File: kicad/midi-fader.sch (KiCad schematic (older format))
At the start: 0 parts

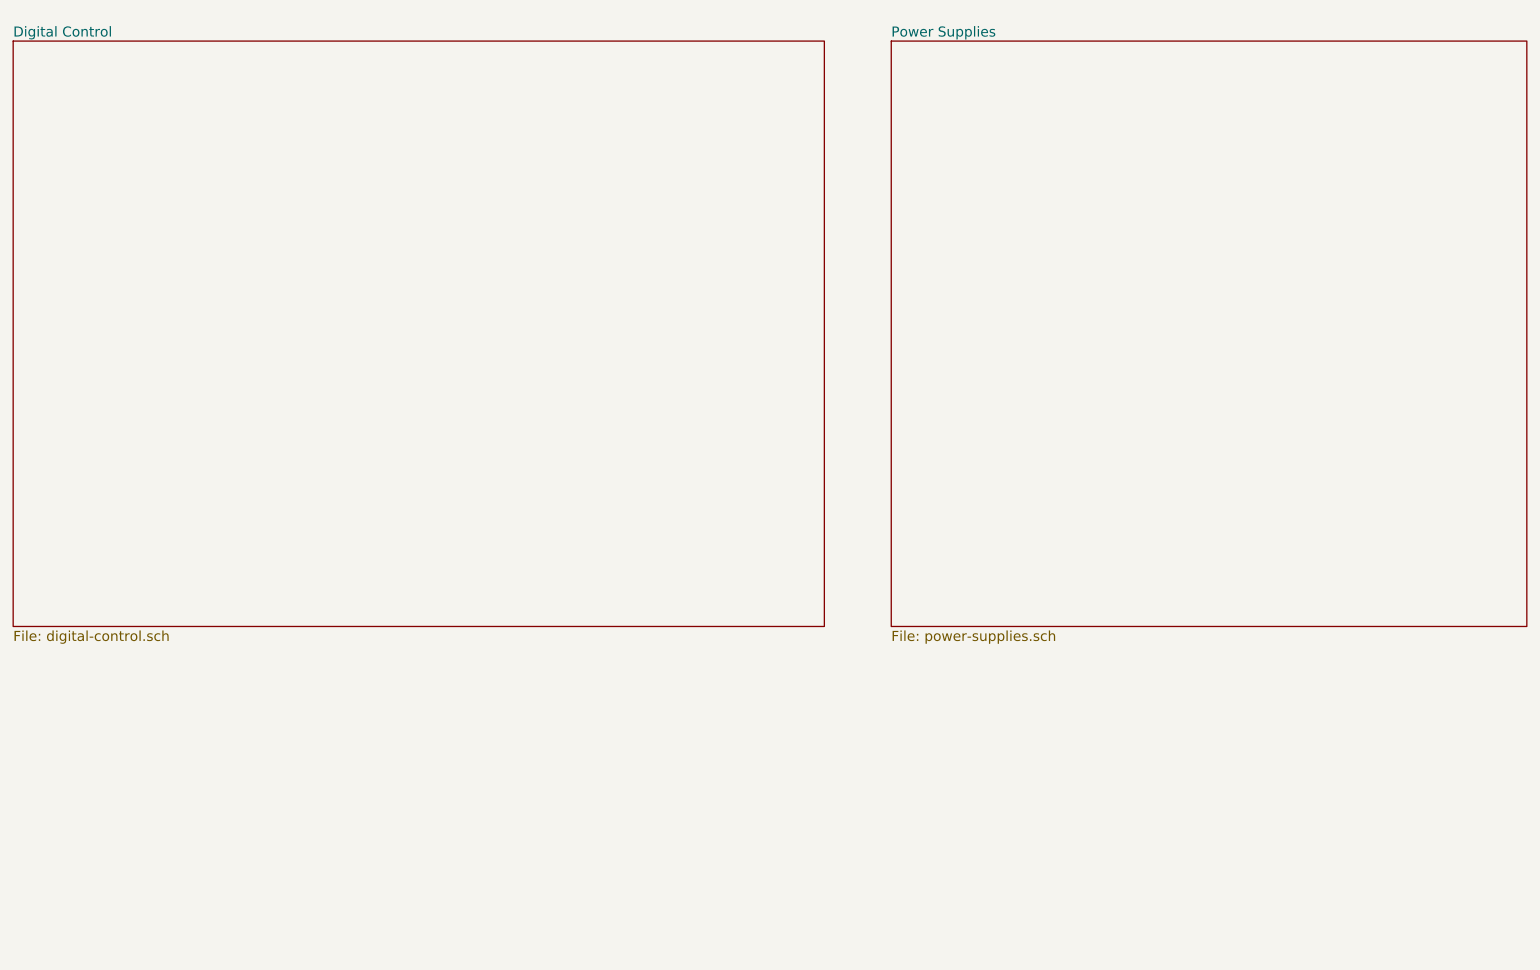
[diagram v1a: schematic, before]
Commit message: Restructured schematic to have a separate input page
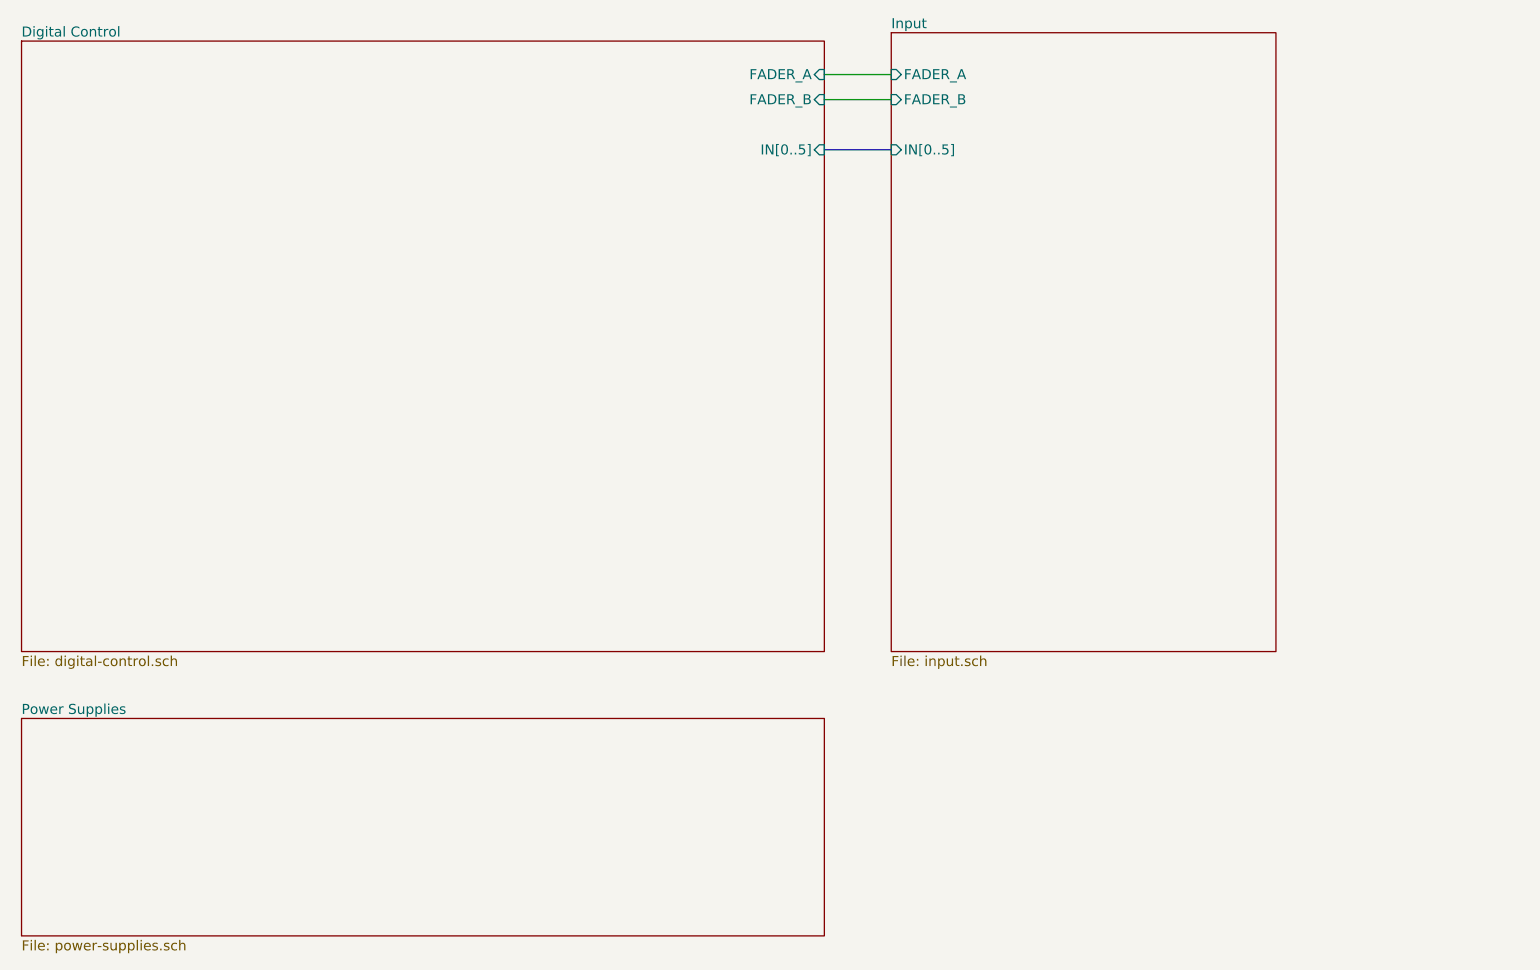
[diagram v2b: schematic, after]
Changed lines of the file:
@@
 $Descr A4 11693 8268
 encoding utf-8
-Sheet 1 3
+Sheet 1 4
 Title ""
 Date ""
@@
 $EndDescr
 $Sheet
-S 1150 1350 4850 3500
+S 1200 1350 4800 3650
 U 5B3C3C50
 F0 "Digital Control" 60
 F1 "digital-control.sch" 60
+F2 "IN[0..5]" I R 6000 2000 60
+F3 "FADER_A" I R 6000 1550 60
+F4 "FADER_B" I R 6000 1700 60
 $EndSheet
 $Sheet
-S 6400 1350 3800 3500
+S 1200 5400 4800 1300
 U 5B3C3C5C
 F0 "Power Supplies" 60
 F1 "power-supplies.sch" 60
 $EndSheet
+$Sheet
+S 6400 1300 2300 3700
+U 5B4048F0
+F0 "Input" 60
+F1 "input.sch" 60
+F2 "IN[0..5]" I L 6400 2000 60
+F3 "FADER_A" I L 6400 1550 60
+F4 "FADER_B" I L 6400 1700 60
+$EndSheet
+Wire Wire Line
+	6000 1550 6400 1550
+Wire Wire Line
+	6400 1700 6000 1700
+Wire Bus Line
+	6000 2000 6400 2000
 $EndSCHEMATC

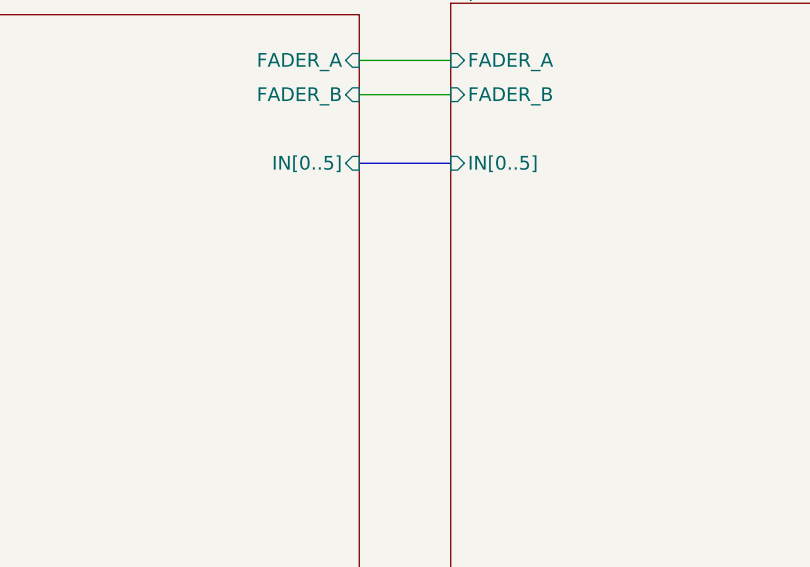
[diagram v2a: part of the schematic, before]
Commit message: Created shift register circuitry and imported footprints
I think 5MHz to 10MHz is the theoretical maximum of this circuit. Actual
frequency will probably be around 5MHz or somewhat less given the signal
integrity issues on a 2-layer board with this many plane breaks.

Created footprints for button and HTSSOP

The HTSSOP footprint is special because I plan to hand solder, so I
added excessive thermal vias and a bare pad on the backside.

The netlist is imported to the PCB, but only the switches are placed.
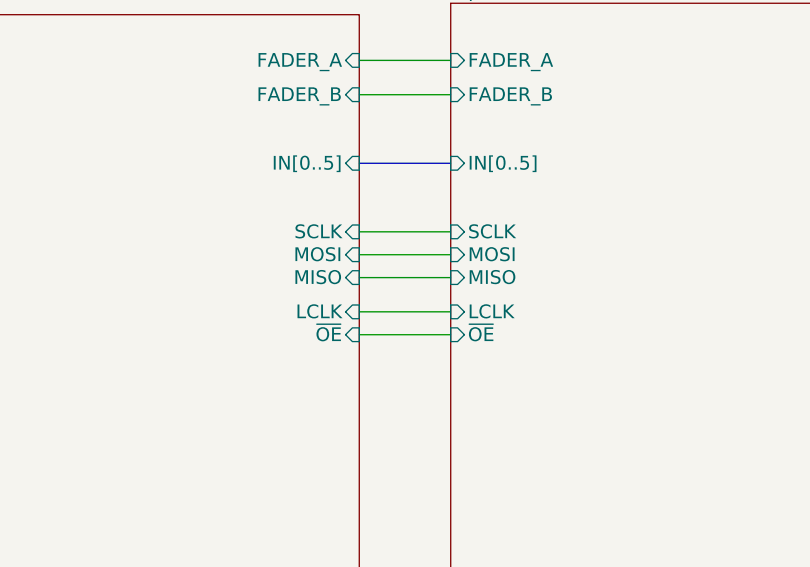
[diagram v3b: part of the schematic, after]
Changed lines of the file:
@@
 F3 "FADER_A" I R 6000 1550 60
 F4 "FADER_B" I R 6000 1700 60
+F5 "SCLK" I R 6000 2300 60
+F6 "MOSI" I R 6000 2400 60
+F7 "MISO" I R 6000 2500 60
+F8 "LCLK" I R 6000 2650 60
+F9 "~OE" I R 6000 2750 60
 $EndSheet
 $Sheet
@@
 F3 "FADER_A" I L 6400 1550 60
 F4 "FADER_B" I L 6400 1700 60
+F5 "SCLK" I L 6400 2300 60
+F6 "MISO" I L 6400 2500 60
+F7 "MOSI" I L 6400 2400 60
+F8 "LCLK" I L 6400 2650 60
+F9 "~OE" I L 6400 2750 60
 $EndSheet
 Wire Wire Line
@@
 Wire Bus Line
 	6000 2000 6400 2000
+Wire Wire Line
+	6000 2300 6400 2300
+Wire Wire Line
+	6000 2400 6400 2400
+Wire Wire Line
+	6000 2500 6400 2500
+Wire Wire Line
+	6400 2650 6000 2650
+Wire Wire Line
+	6000 2750 6400 2750
 $EndSCHEMATC
